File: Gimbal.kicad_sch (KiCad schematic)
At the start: 51 parts, among them J1 XT60-M, J2 USB_C_Receptacle_USB2.0, J3 0022232041, J4 0022232041, J5 0022232041, J6 Conn_01x02, SW1 SW_Push, SW2 SW_Push, U1 ESP32-S2-SOLO, U2 BMI088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

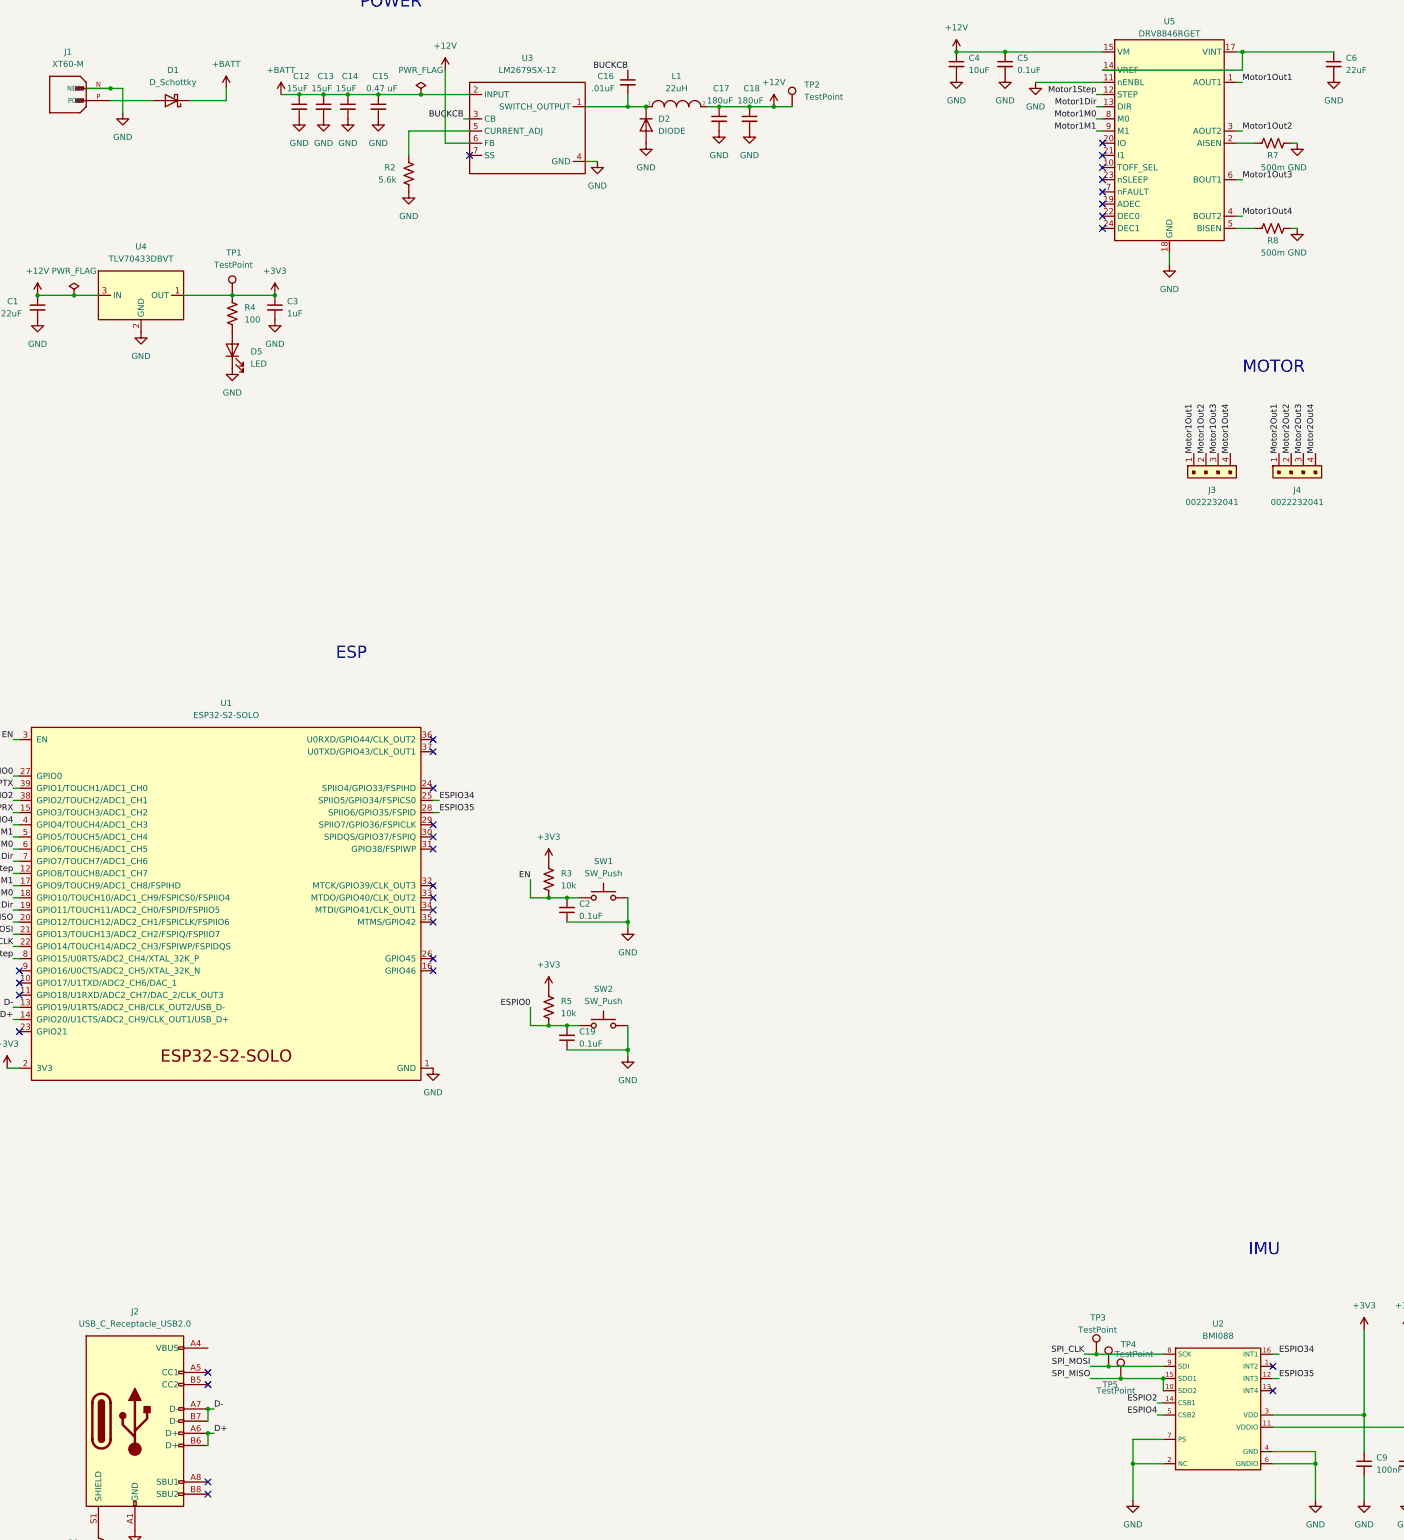
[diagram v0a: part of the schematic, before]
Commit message: updated layout and schematic to fix errors
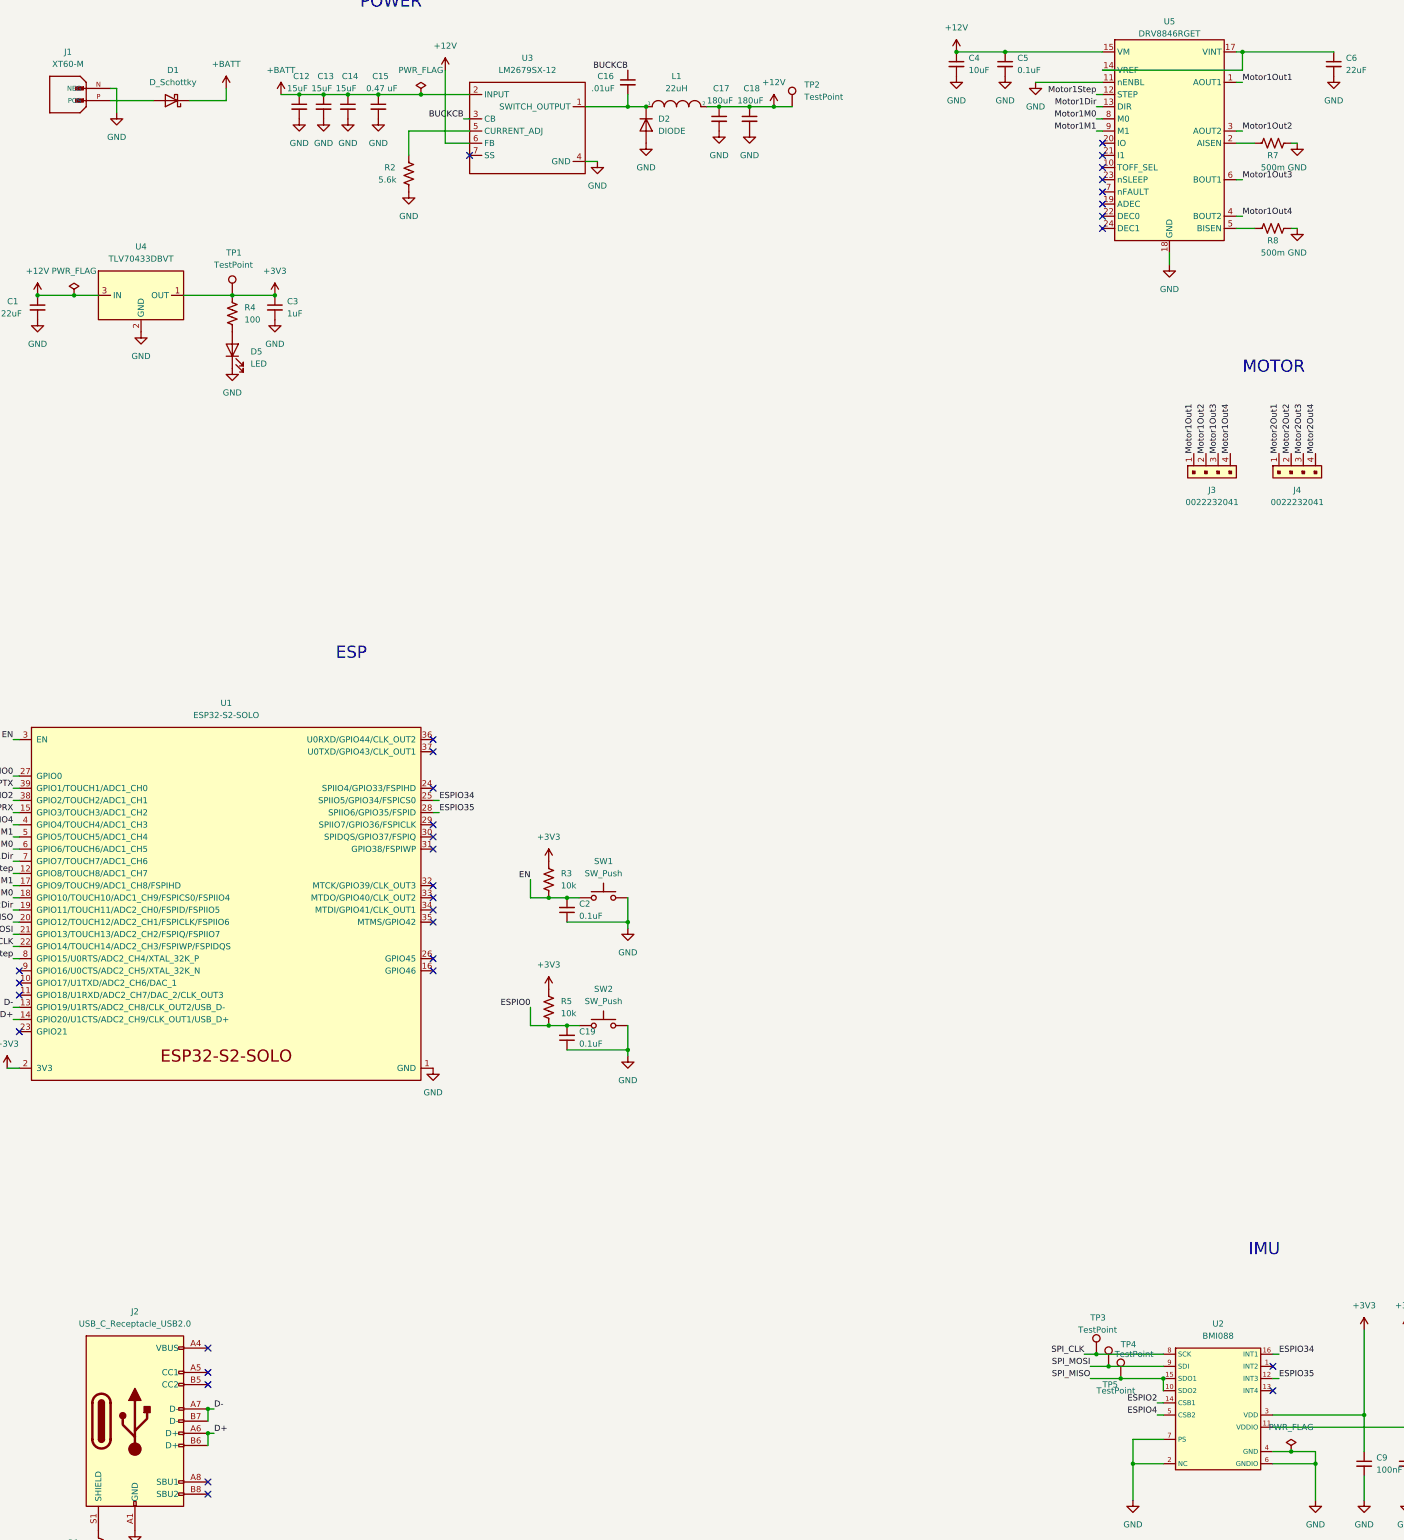
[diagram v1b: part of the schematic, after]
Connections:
- no-connect marks 40 -> 41
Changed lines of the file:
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@@
   (junction (at 107.95 60.96) (diameter 0) (color 0 0 0 0)
   )
-  (junction (at 52.07 59.69) (diameter 0) (color 0 0 0 0)
-  )
   (junction (at 160.02 233.68) (diameter 0) (color 0 0 0 0)
   )
@@
   )
   (junction (at 101.6 60.96) (diameter 0) (color 0 0 0 0)
+  )
+  (junction (at 298.45 344.17) (diameter 0) (color 0 0 0 0)
   )
   (no_connect (at 358.14 80.01))
@@
   (no_connect (at 259.08 78.74))
   (no_connect (at 259.08 83.82))
+  (no_connect (at 72.39 322.58))
   (no_connect (at 33.02 248.92))
   (no_connect (at 294.64 331.47))
@@
     (stroke (width 0) (type default) (color 0 0 0 0))
   )
+  (wire (pts (xy 53.34 59.69) (xy 52.07 59.69))
+    (stroke (width 0) (type default) (color 0 0 0 0))
+  )
   (wire (pts (xy 33.02 223.52) (xy 31.75 223.52))
     (stroke (width 0) (type default) (color 0 0 0 0))
@@
     (stroke (width 0) (type default) (color 0 0 0 0))
   )
-  (wire (pts (xy 46.99 59.69) (xy 52.07 59.69))
-    (stroke (width 0) (type default) (color 0 0 0 0))
-  )
   (wire (pts (xy 147.32 260.35) (xy 160.02 260.35))
     (stroke (width 0) (type default) (color 0 0 0 0))
@@
     (stroke (width 0) (type default) (color 0 0 0 0))
   )
+  (wire (pts (xy 298.45 344.17) (xy 303.53 344.17))
+    (stroke (width 0) (type default) (color 0 0 0 0))
+  )
   (wire (pts (xy 287.02 78.74) (xy 288.29 78.74))
     (stroke (width 0) (type default) (color 0 0 0 0))
@@
     (stroke (width 0) (type default) (color 0 0 0 0))
   )
-  (wire (pts (xy 52.07 59.69) (xy 54.61 59.69))
-    (stroke (width 0) (type default) (color 0 0 0 0))
-  )
   (wire (pts (xy 72.39 335.28) (xy 72.39 337.82))
     (stroke (width 0) (type default) (color 0 0 0 0))
@@
     (stroke (width 0) (type default) (color 0 0 0 0))
   )
-  (wire (pts (xy 54.61 59.69) (xy 54.61 64.77))
-    (stroke (width 0) (type default) (color 0 0 0 0))
-  )
   (wire (pts (xy 91.44 60.96) (xy 96.52 60.96))
     (stroke (width 0) (type default) (color 0 0 0 0))
@@
     (stroke (width 0) (type default) (color 0 0 0 0))
   )
-  (wire (pts (xy 294.64 344.17) (xy 303.53 344.17))
+  (wire (pts (xy 294.64 344.17) (xy 298.45 344.17))
     (stroke (width 0) (type default) (color 0 0 0 0))
   )
@@
   )
   (wire (pts (xy 72.39 335.28) (xy 73.66 335.28))
+    (stroke (width 0) (type default) (color 0 0 0 0))
+  )
+  (wire (pts (xy 53.34 59.69) (xy 53.34 64.77))
     (stroke (width 0) (type default) (color 0 0 0 0))
   )
@@
     (pin "2")
   )
-  (symbol (lib_id "power:GND") (at 54.61 64.77 0) (unit 1)
-    (in_bom yes) (on_board yes) (fields_autoplaced)
-    (property "Reference" "#PWR0112" (id 0) (at 54.61 71.12 0)
-      (effects (font (size 1.27 1.27)) hide)
-    )
-    (property "Value" "GND" (id 1) (at 54.61 69.85 0))
-    (property "Footprint" "" (id 2) (at 54.61 64.77 0)
-      (effects (font (size 1.27 1.27)) hide)
-    )
-    (property "Datasheet" "" (id 3) (at 54.61 64.77 0)
+  (symbol (lib_id "power:GND") (at 53.34 64.77 0) (unit 1)
+    (in_bom yes) (on_board yes) (fields_autoplaced)
+    (property "Reference" "#PWR0112" (id 0) (at 53.34 71.12 0)
+      (effects (font (size 1.27 1.27)) hide)
+    )
+    (property "Value" "GND" (id 1) (at 53.34 69.85 0))
+    (property "Footprint" "" (id 2) (at 53.34 64.77 0)
+      (effects (font (size 1.27 1.27)) hide)
+    )
+    (property "Datasheet" "" (id 3) (at 53.34 64.77 0)
+      (effects (font (size 1.27 1.27)) hide)
+    )
+    (pin "1")
+  )
+  (symbol (lib_id "power:PWR_FLAG") (at 298.45 344.17 0) (unit 1)
+    (in_bom yes) (on_board yes) (fields_autoplaced)
+    (property "Reference" "#FLG0103" (id 0) (at 298.45 342.265 0)
+      (effects (font (size 1.27 1.27)) hide)
+    )
+    (property "Value" "PWR_FLAG" (id 1) (at 298.45 339.09 0))
+    (property "Footprint" "" (id 2) (at 298.45 344.17 0)
+      (effects (font (size 1.27 1.27)) hide)
+    )
+    (property "Datasheet" "~" (id 3) (at 298.45 344.17 0)
       (effects (font (size 1.27 1.27)) hide)
     )
@@
       (reference "#FLG0102") (unit 1) (value "PWR_FLAG") (footprint "")
     )
+    (path "/ca93ad39-5b7b-4abe-ac93-4dc4909c78e8"
+      (reference "#FLG0103") (unit 1) (value "PWR_FLAG") (footprint "")
+    )
     (path "/fcbb3eca-b824-4538-81ce-a9641c21bef7"

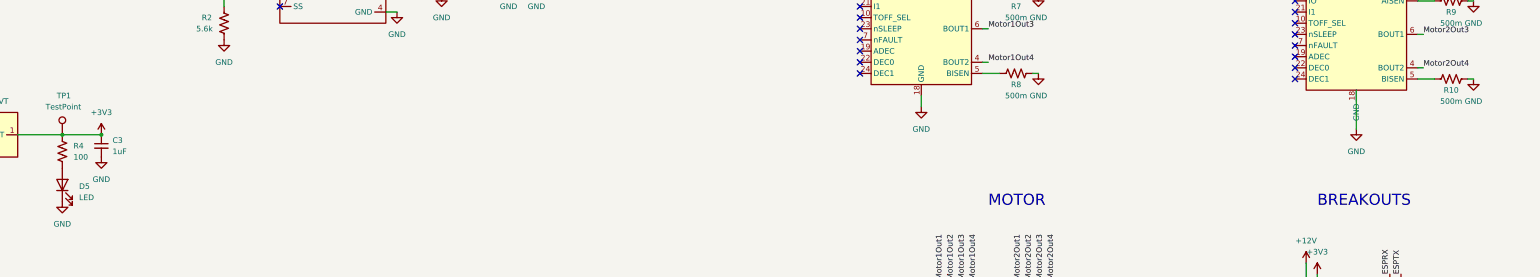
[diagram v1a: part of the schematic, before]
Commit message: Changed numbering
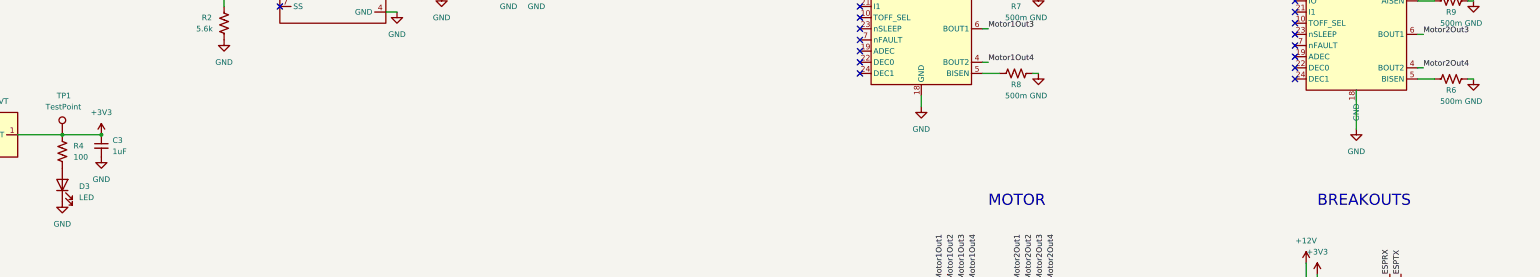
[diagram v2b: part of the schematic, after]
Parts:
- renumbered D5 to D3, R10 to R6
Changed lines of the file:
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@@
   (symbol (lib_id "Device:LED") (at 77.47 114.3 90) (unit 1)
     (in_bom yes) (on_board yes) (fields_autoplaced)
-    (property "Reference" "D5" (id 0) (at 81.28 114.6174 90)
+    (property "Reference" "D3" (id 0) (at 81.28 114.6174 90)
       (effects (font (size 1.27 1.27)) (justify right))
     )
@@
   (symbol (lib_id "Device:R_US") (at 393.7 90.17 90) (unit 1)
     (in_bom yes) (on_board yes)
-    (property "Reference" "R10" (id 0) (at 393.7 92.71 90))
+    (property "Reference" "R6" (id 0) (at 393.7 92.71 90))
     (property "Value" "500m" (id 1) (at 393.7 95.25 90))
     (property "Footprint" "Resistor_SMD:R_0805_2012Metric" (id 2) (at 393.954 89.154 90)
@@
     )
     (path "/668de95b-5ac6-43e3-9997-9750d45aadc1"
-      (reference "D5") (unit 1) (value "LED") (footprint "LED_SMD:LED_0805_2012Metric")
+      (reference "D3") (unit 1) (value "LED") (footprint "LED_SMD:LED_0805_2012Metric")
     )
     (path "/46c8c91f-27ea-4db3-8ff9-8a8bda90287a"
@@
       (reference "R5") (unit 1) (value "10k") (footprint "Resistor_SMD:R_0805_2012Metric")
     )
+    (path "/6deb4374-0d6e-4556-88ed-01064edb6f4b"
+      (reference "R6") (unit 1) (value "500m") (footprint "Resistor_SMD:R_0805_2012Metric")
+    )
     (path "/0bb95235-3024-483f-86a5-45f3fad29f52"
       (reference "R7") (unit 1) (value "500m") (footprint "Resistor_SMD:R_0805_2012Metric")
@@
       (reference "R9") (unit 1) (value "500m") (footprint "Resistor_SMD:R_0805_2012Metric")
     )
-    (path "/6deb4374-0d6e-4556-88ed-01064edb6f4b"
-      (reference "R10") (unit 1) (value "500m") (footprint "Resistor_SMD:R_0805_2012Metric")
-    )
     (path "/e7ff2abd-f6da-4a2c-a822-bb8a1844752a"

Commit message: layout completed
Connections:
- net GND: now also J2.A4 (VBUS), J2.A9 (VBUS), J2.B4 (VBUS), J2.B9 (VBUS)
- no-connect marks 41 -> 40
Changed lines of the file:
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@@
   (no_connect (at 259.08 78.74))
   (no_connect (at 259.08 83.82))
-  (no_connect (at 72.39 322.58))
   (no_connect (at 33.02 248.92))
   (no_connect (at 294.64 331.47))
@@
   )
   (wire (pts (xy 260.35 326.39) (xy 271.78 326.39))
+    (stroke (width 0) (type default) (color 0 0 0 0))
+  )
+  (wire (pts (xy 72.39 322.58) (xy 74.93 322.58))
     (stroke (width 0) (type default) (color 0 0 0 0))
   )
@@
     (pin "1")
   )
+  (symbol (lib_id "power:GND") (at 74.93 322.58 0) (unit 1)
+    (in_bom yes) (on_board yes) (fields_autoplaced)
+    (property "Reference" "#PWR0154" (id 0) (at 74.93 328.93 0)
+      (effects (font (size 1.27 1.27)) hide)
+    )
+    (property "Value" "GND" (id 1) (at 74.93 327.66 0))
+    (property "Footprint" "" (id 2) (at 74.93 322.58 0)
+      (effects (font (size 1.27 1.27)) hide)
+    )
+    (property "Datasheet" "" (id 3) (at 74.93 322.58 0)
+      (effects (font (size 1.27 1.27)) hide)
+    )
+    (pin "1")
+  )
   (symbol (lib_id "power:GND") (at 114.3 81.28 0) (unit 1)
     (in_bom yes) (on_board yes) (fields_autoplaced)
@@
       (reference "#PWR0153") (unit 1) (value "GND") (footprint "")
     )
+    (path "/856a52fa-07d1-41b3-9105-fa44da7ce871"
+      (reference "#PWR0154") (unit 1) (value "GND") (footprint "")
+    )
     (path "/95cd3f9f-62c1-468e-9608-efa5dd986aec"

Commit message: comment
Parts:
- removed J2: USB_C_Receptacle_USB2.0, Connector_USB:USB_C_Receptacle_Amphenol_12401610E4-2A, symbol Connector:USB_C_Receptacle_USB2.0
- added J2: USB_C_Receptacle, symbol Connector:USB_C_Receptacle
- added R10, R11: 10k, Resistor_SMD:R_0805_2012Metric, symbol Device:R_US
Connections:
- net D+: now also J2.A6 (D+), J2.B6 (D+)
- net D-: now also J2.A7 (D-), J2.B7 (D-)
- net GND: now also J2.A1 (GND), J2.A12 (GND), J2.B1 (GND), J2.B12 (GND), R10.2, R11.2
- net at R1.1: now also J2.S1 (SHIELD)
- new net: J2.B5 (CC2), R10.1
- new net: J2.A5 (CC1), R11.1
- new net: J2.A4 (VBUS), J2.A9 (VBUS), J2.B4 (VBUS), J2.B9 (VBUS)
- no-connect marks 40 -> 47

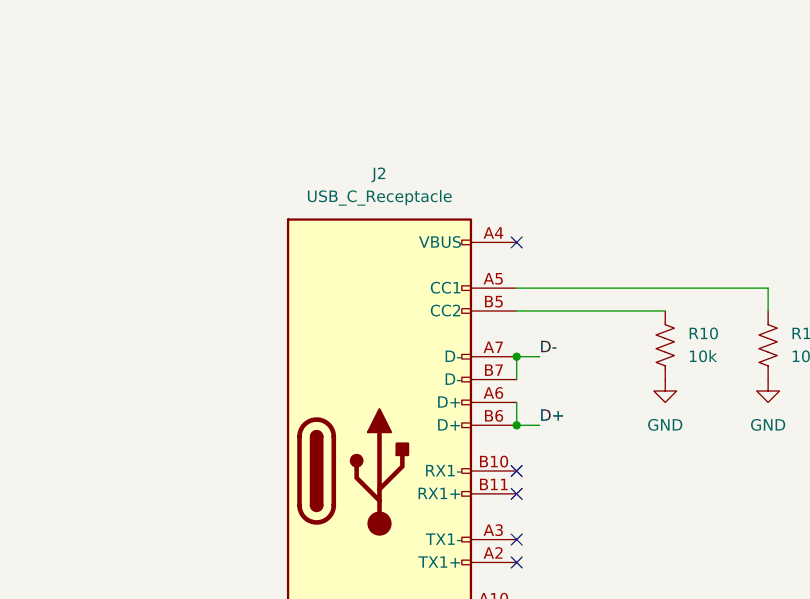
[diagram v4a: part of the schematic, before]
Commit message: Fixed USB connector issues
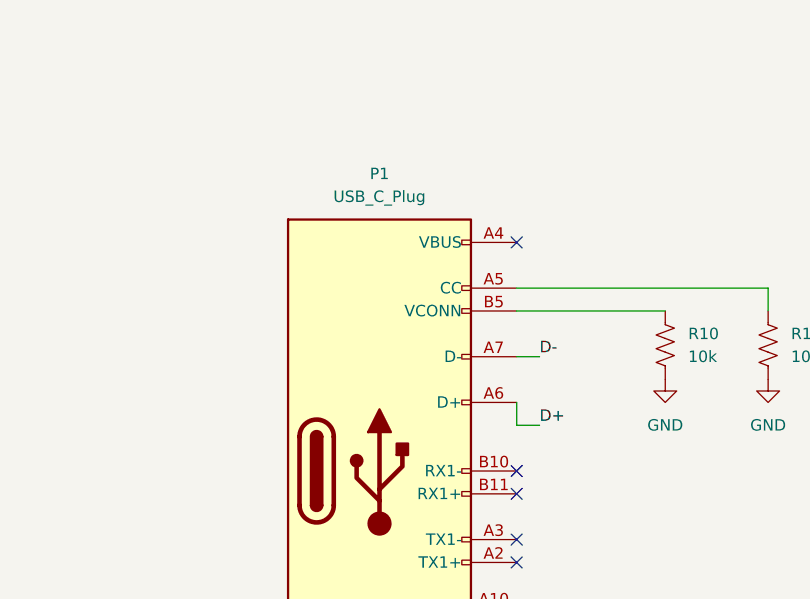
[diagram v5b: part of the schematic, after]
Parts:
- removed J2: USB_C_Receptacle, symbol Connector:USB_C_Receptacle
- added P1: USB_C_Plug, Connector_USB:USB_C_Receptacle_JAE_DX07S016JA1R1500, symbol Connector:USB_C_Plug
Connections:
- net D+: now also P1.A6 (D+)
- net D-: now also P1.A7 (D-)
- net GND: now also P1.A1 (GND), P1.A12 (GND), P1.B1 (GND), P1.B12 (GND)
- net at R1.1: now also P1.S1 (SHIELD)
- net at R10.1: now also P1.B5 (VCONN)
- net at R11.1: now also P1.A5 (CC)
- new net: P1.A4 (VBUS), P1.A9 (VBUS), P1.B4 (VBUS), P1.B9 (VBUS)
